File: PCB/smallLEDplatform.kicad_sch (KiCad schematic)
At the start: 33 parts, among them J101 USB_C_Receptacle, J102 Conn_02x05_Odd_Even, J103 Conn_01x03_Male, J104 Conn_01x03_Male, Q101 AO3400A, U101 STM32G0B1CBTx, U102 USBLC6-2P6, U103 TCPP01-M12

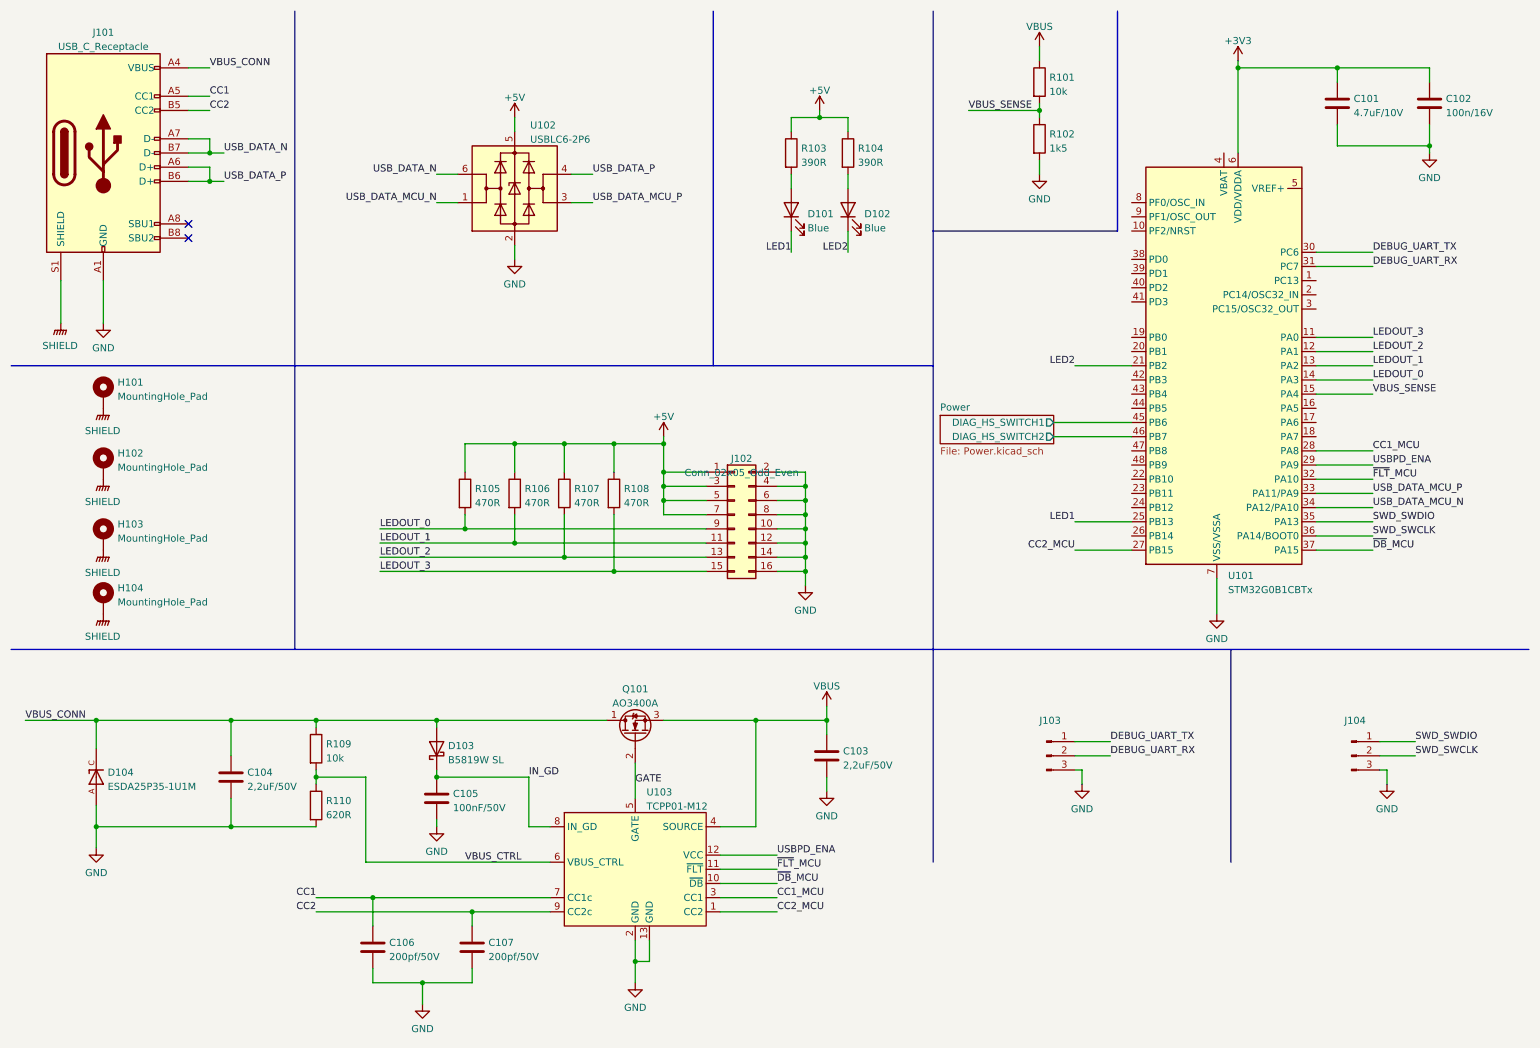
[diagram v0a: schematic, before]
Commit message: Add a new DC/DC solution to the schematic
Components has been added to layout, but not properly done
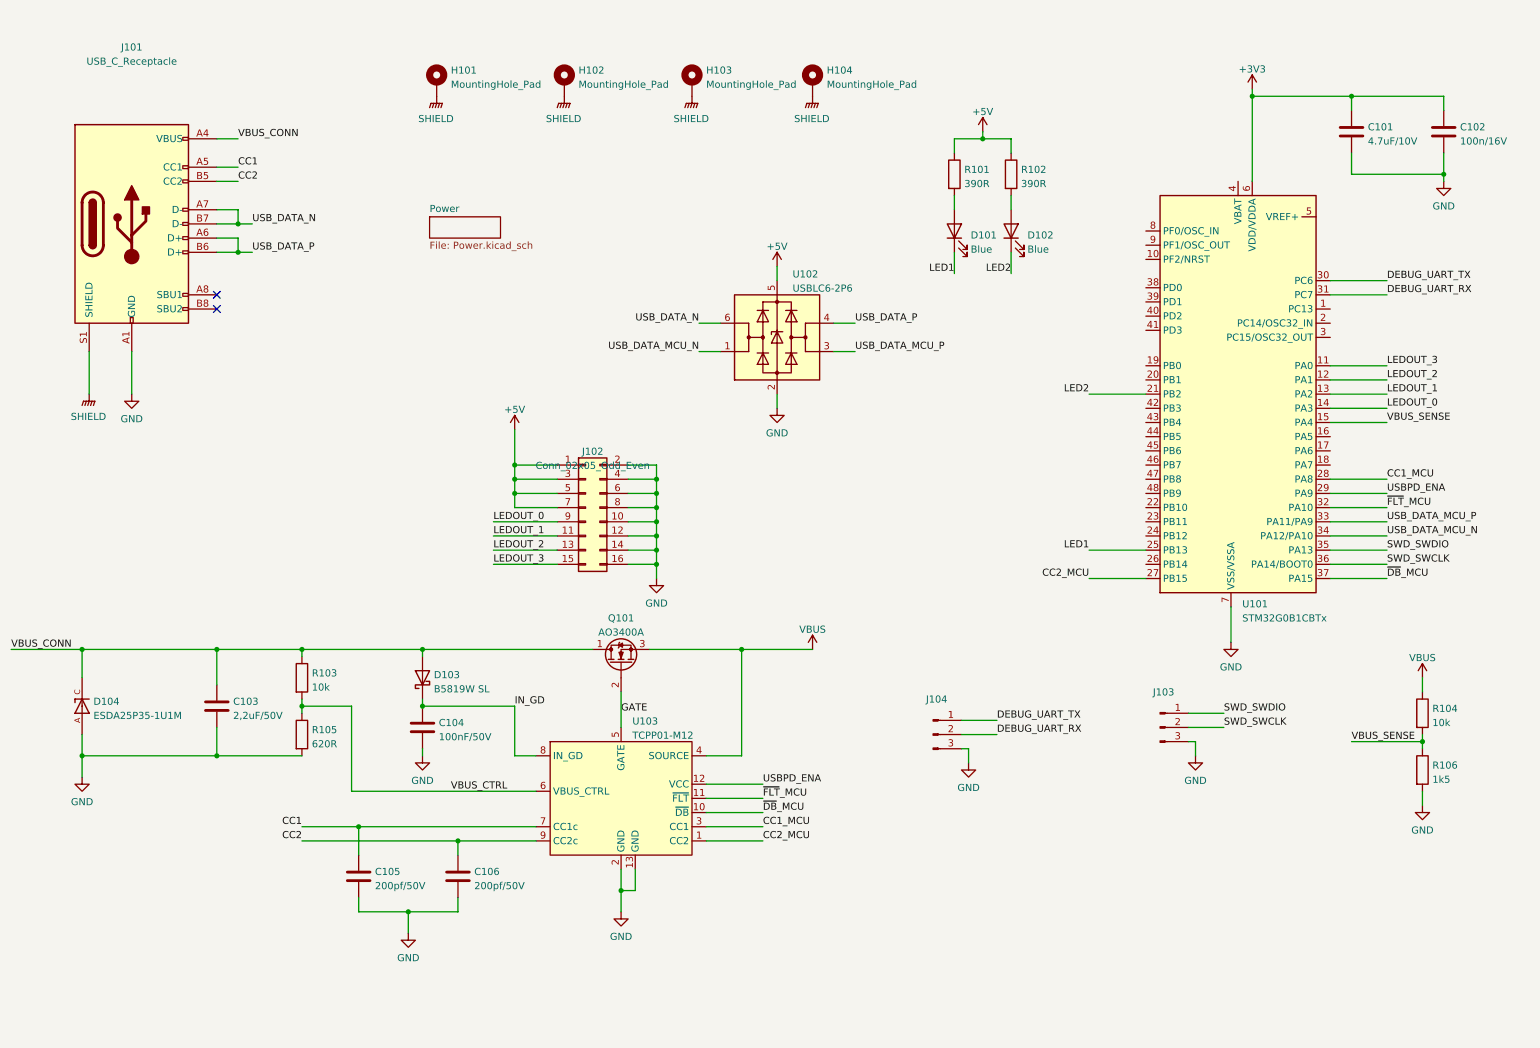
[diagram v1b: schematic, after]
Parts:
- removed C103: 2,2uF/50V, Capacitor_SMD:C_0805_2012Metric, symbol Device:C
- removed R105, R106, R107, R108: 470R, Resistor_SMD:R_0402_1005Metric, symbol Device:R
- C104: renamed from C105; footprint Capacitor_SMD:C_0402_1005Metric -> Capacitor_SMD:C_0603_1608Metric_Pad1.08x0.95mm_HandSolder; LCSC C307331 -> (none)
- D101, D102: LCSC C72041 -> (none)
- renumbered C104 to C103, C106 to C105, C107 to C106, J104 to J103, J103 to J104, R103 to R101, R104 to R102, R109 to R103, R101 to R104, R110 to R105, R102 to R106
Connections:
- net Power/DIAG_HS_SWITCH1: no longer names the net of U101.45 (PB6)
- net Power/DIAG_HS_SWITCH2: no longer names the net of U101.46 (PB7)
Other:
- sheet Power ports: added none; removed DIAG_HS_SWITCH1, DIAG_HS_SWITCH2
- moved on the sheet: C101, C102, C103, C104, C105, C106, D101, D102, D103, D104, H101, H102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
